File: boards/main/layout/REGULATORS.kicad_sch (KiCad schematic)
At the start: 41 parts, among them IC7 L6981C33DR, J1 B02B-PASK(LF)(SN), Q6 HSBB3072, SW4 MK-12D18-G040, U1 TPS61178RNWR, U4 TPS2121RUXR, U5 LM66100DCKR

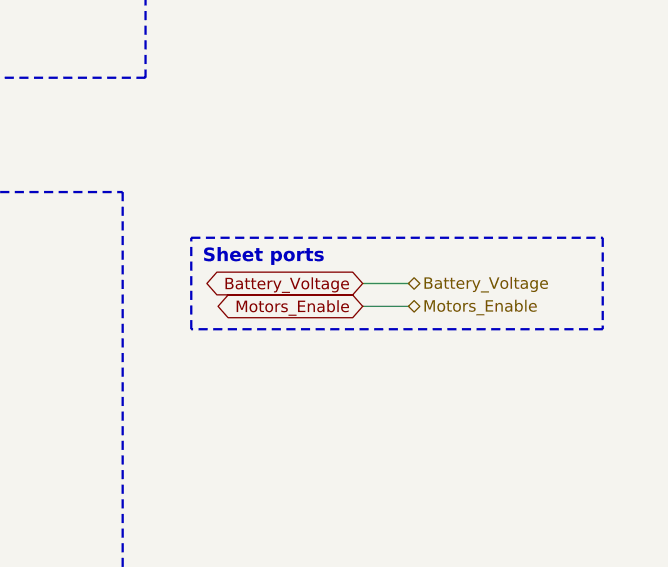
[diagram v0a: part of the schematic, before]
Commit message: 🎨 Place the main board's SENSORS sheet, and size the ports column for global labels' flags
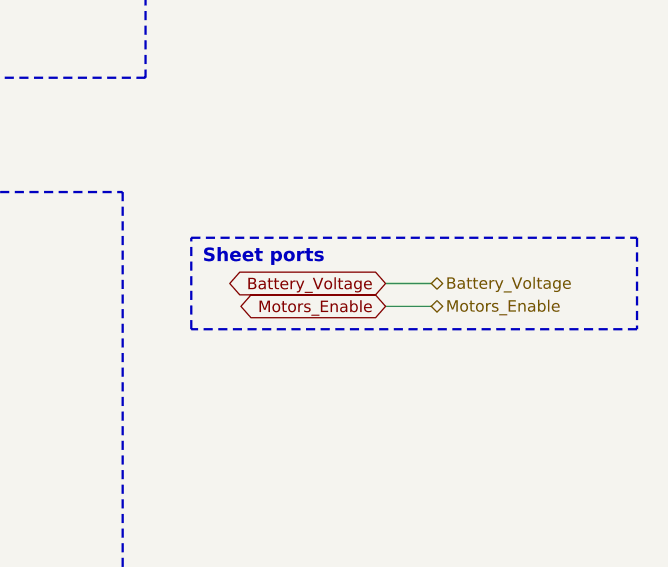
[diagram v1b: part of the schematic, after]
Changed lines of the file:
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@@
 	(wire
 		(pts
-			(xy 339.09 78.74) (xy 344.17 78.74)
+			(xy 341.63 78.74) (xy 346.71 78.74)
 		)
 		(stroke
@@
 	(wire
 		(pts
-			(xy 339.09 81.28) (xy 344.17 81.28)
+			(xy 341.63 81.28) (xy 346.71 81.28)
 		)
 		(stroke
@@
 	(global_label "Battery_Voltage"
 		(shape bidirectional)
-		(at 339.09 78.74 180)
+		(at 341.63 78.74 180)
 		(effects
 			(font
@@
 		)
 		(property "Intersheetrefs" "${INTERSHEET_REFS}"
-			(at 339.09 78.74 0)
+			(at 341.63 78.74 0)
 			(hide yes)
 			(show_name no)
@@
 	(hierarchical_label "Battery_Voltage"
 		(shape bidirectional)
-		(at 344.17 78.74 0)
+		(at 346.71 78.74 0)
 		(effects
 			(font
@@
 	(global_label "Motors_Enable"
 		(shape bidirectional)
-		(at 339.09 81.28 180)
+		(at 341.63 81.28 180)
 		(effects
 			(font
@@
 		)
 		(property "Intersheetrefs" "${INTERSHEET_REFS}"
-			(at 339.09 81.28 0)
+			(at 341.63 81.28 0)
 			(hide yes)
 			(show_name no)
@@
 	(hierarchical_label "Motors_Enable"
 		(shape bidirectional)
-		(at 344.17 81.28 0)
+		(at 346.71 81.28 0)
 		(effects
 			(font
@@
 	(rectangle
 		(start 320.04 73.66)
-		(end 365.76 83.82)
+		(end 369.57 83.82)
 		(stroke
 			(width 0.254)
